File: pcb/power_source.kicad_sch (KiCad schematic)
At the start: 5 parts, among them J6 USB4110-GF-A

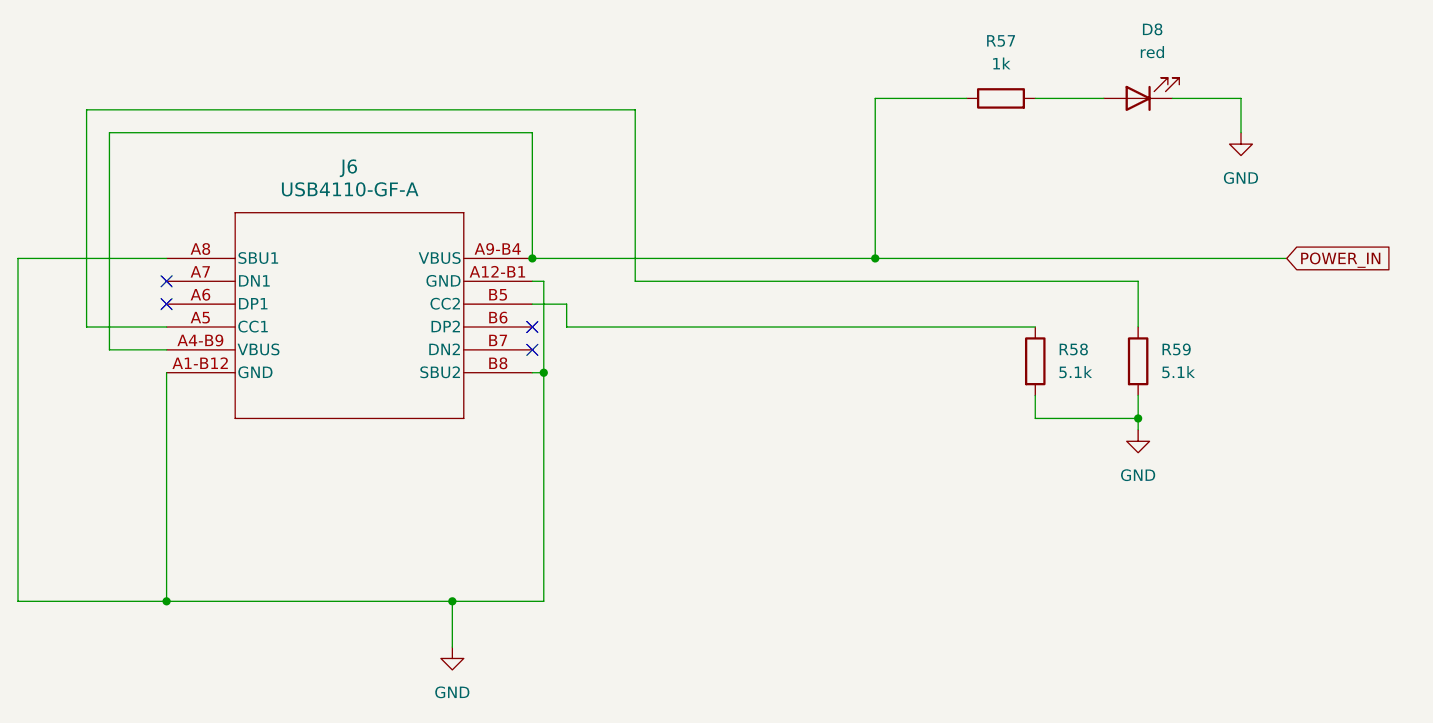
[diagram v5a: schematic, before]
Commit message: fix usb symbol
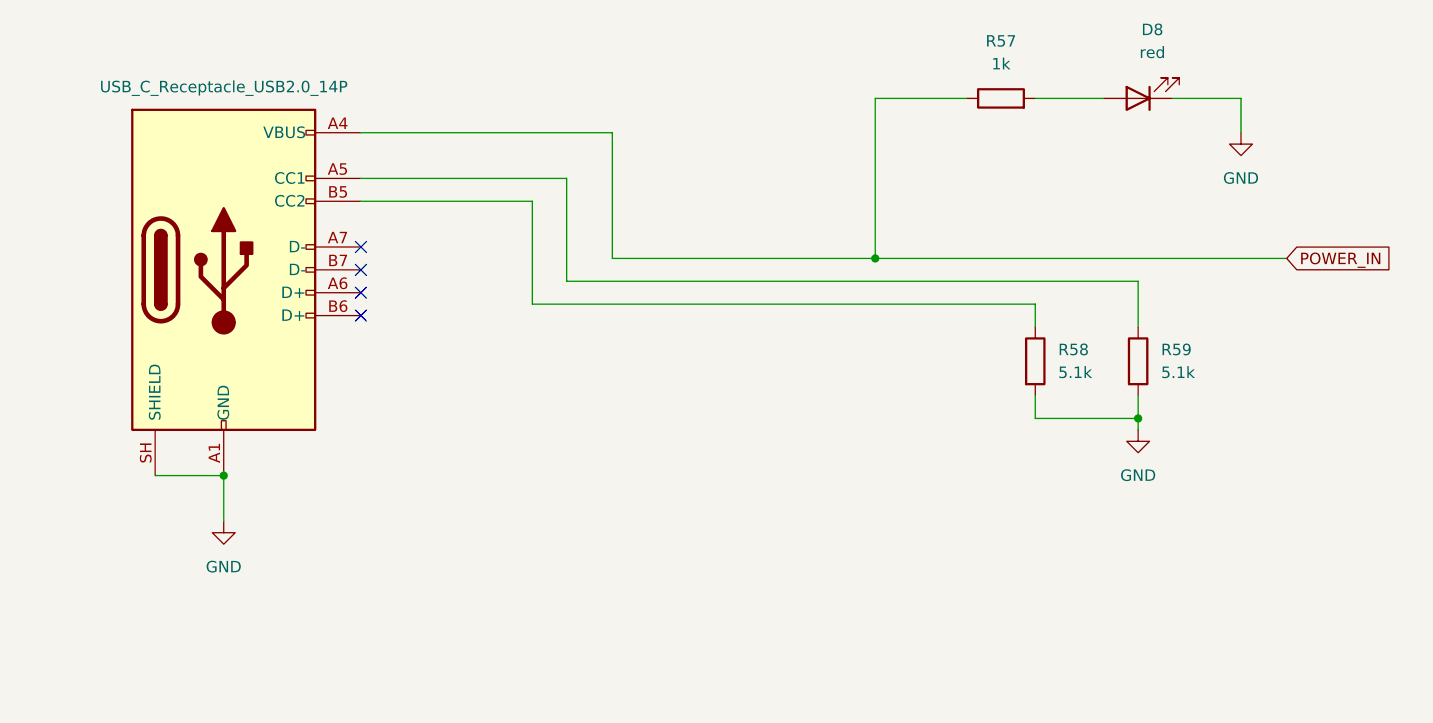
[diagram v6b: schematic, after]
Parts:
- removed J6: USB4110-GF-A, USB4110-GF-A_GCT, symbol USB4110_GF_A:USB4110-GF-A
- added J7: USB_C_Receptacle_USB2.0_14P, USB4110_GF_A:USB4110-GF-A_GCT, symbol Connector:USB_C_Receptacle_USB2.0_14P
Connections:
- net GND: now also J7.A1 (GND), J7.A12 (GND), J7.B1 (GND), J7.B12 (GND), J7.SH (SHIELD)
- net POWER_IN: now also J7.A4 (VBUS), J7.A9 (VBUS), J7.B4 (VBUS), J7.B9 (VBUS)
- net at R59.1: now also J7.A5 (CC1)
- net at R58.1: now also J7.B5 (CC2)

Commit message: pcb/layout: usbs and pds
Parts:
- J7: footprint USB4110_GF_A:USB4110-GF-A_GCT -> Connector_USB:USB_C_Receptacle_GCT_USB4105-xx-A_16P_TopMnt_Horizontal
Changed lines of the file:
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@@
 			)
 		)
-		(property "Footprint" "USB4110_GF_A:USB4110-GF-A_GCT"
+		(property "Footprint" "Connector_USB:USB_C_Receptacle_GCT_USB4105-xx-A_16P_TopMnt_Horizontal"
 			(at 71.12 62.23 0)
 			(hide yes)

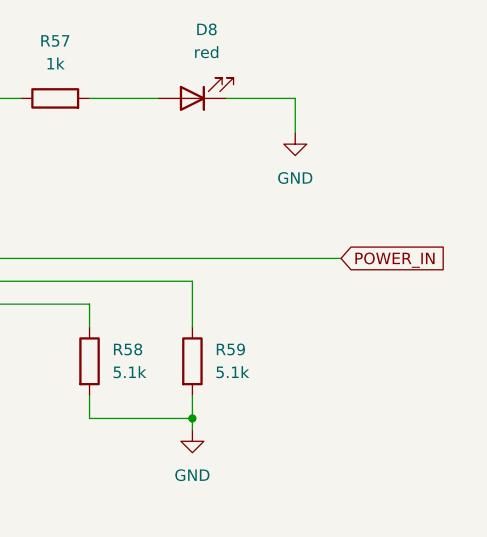
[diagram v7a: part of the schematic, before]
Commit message: added new jumper complete
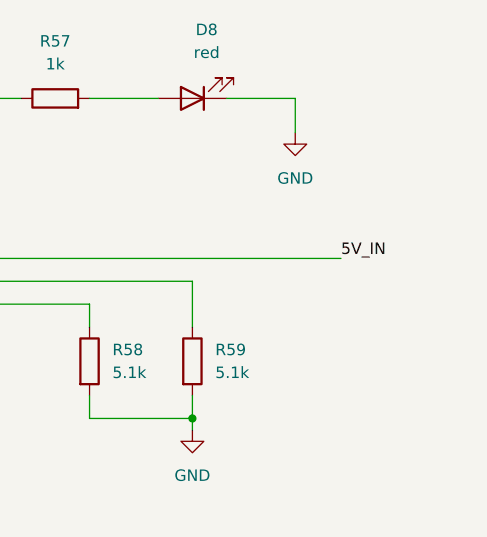
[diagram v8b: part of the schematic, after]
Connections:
- net POWER_IN renamed 5V_IN
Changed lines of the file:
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@@
 		)
 	)
-	(global_label "POWER_IN"
-		(shape input)
+	(label "5V_IN"
 		(at 185.42 60.96 0)
 		(effects
@@
 				(size 1.27 1.27)
 			)
-			(justify left)
-		)
-		(property "Intersheetrefs" "${INTERSHEET_REFS}"
-			(at 197.779 60.96 0)
-			(hide yes)
-			(show_name no)
-			(do_not_autoplace no)
-			(effects
-				(font
-					(size 1.27 1.27)
-				)
-				(justify left)
-			)
-		)
-		(property "Extra" "5V"
-			(at 184.658 57.658 0)
-			(show_name no)
-			(do_not_autoplace no)
-			(effects
-				(font
-					(size 1.27 1.27)
-					(color 15 0 171 1)
-				)
-				(justify left)
-			)
+			(justify left bottom)
 		)
 	)
